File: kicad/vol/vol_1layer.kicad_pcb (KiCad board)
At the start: 2 copper layers, 42 x 26 mm, 6 parts, among them J1 IN L-G-R, J2 OUT L-G-R, J3 LED IN

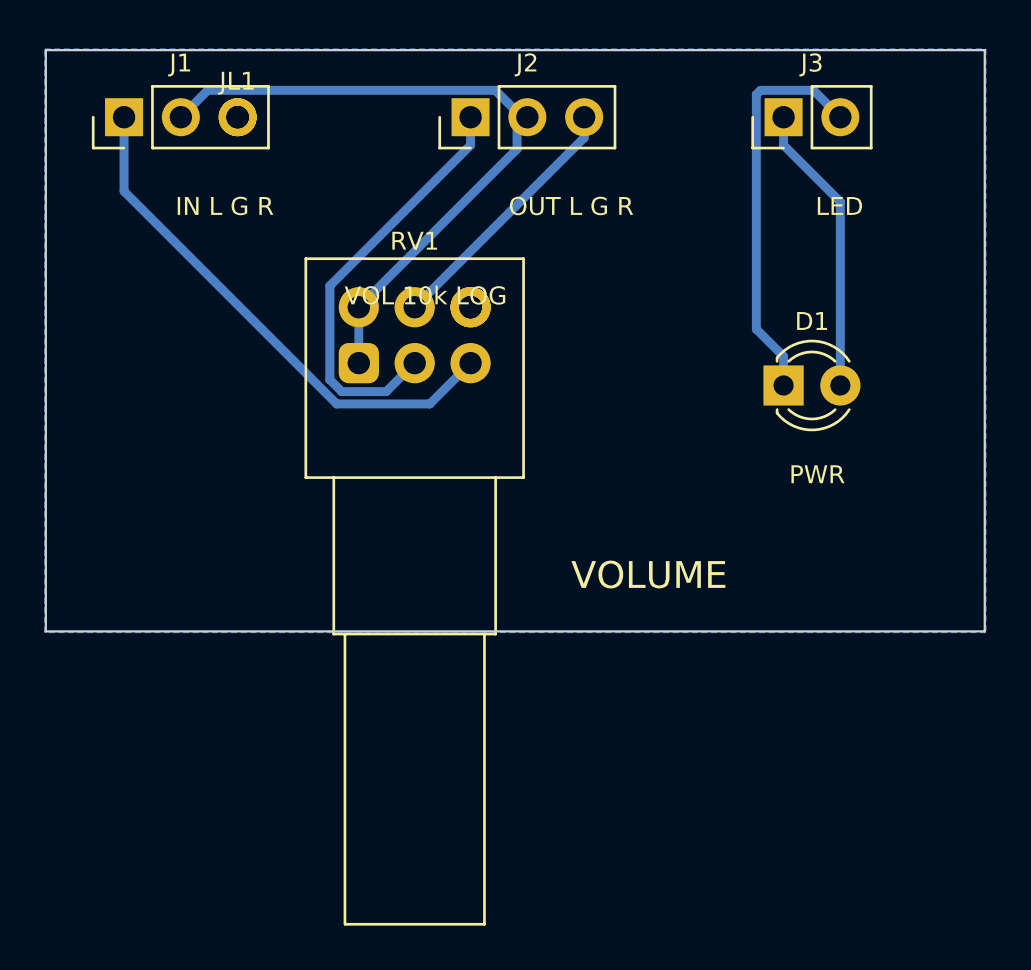
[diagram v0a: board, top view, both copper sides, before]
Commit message: Square 144 x 144 mm panel with rails; amp widened to 134 x 71 mm so PSU plus volume board match its width; readable silkscreen
References sit inside resistor, diode and ceramic outlines along the body axis, larger text; electrolytic,
transistor and test-point labels stay beside the part. Hybrid footprints built from the library parts keep
polarity marks. All 2-layer boards, the panel and the single-sided PSU and volume boards are DRC clean.
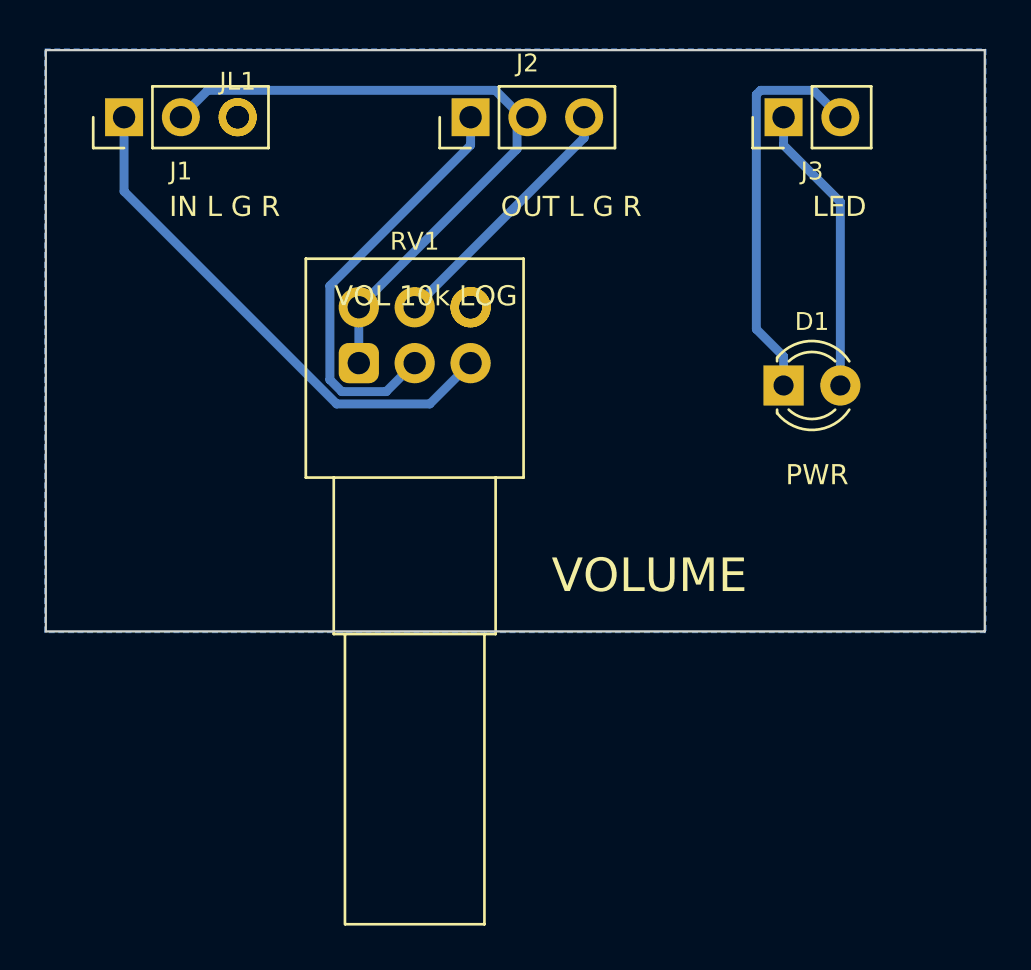
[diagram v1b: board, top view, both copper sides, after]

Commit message: Repository URL and revision on every silkscreen and on the panel rails
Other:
- board text added: "v1.0 2026-10"
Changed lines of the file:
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@@
 		(layer "Edge.Cuts")
+	)
+	(gr_text "v1.0 2026-10"
+		(at 76.95 71.45 0)
+		(layer "F.SilkS")
+		(effects
+			(font
+				(size 0.8 0.8)
+				(thickness 0.12)
+			)
+		)
 	)
 	(gr_text "IN L G R"

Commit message: Release 1.1: square panel, rotated terminals, readable silkscreen, URL and revision stamps
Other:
- board text added: "v1.1 2026-10"
- board text removed: "v1.0 2026-10"
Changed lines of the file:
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@@
 		(layer "Edge.Cuts")
 	)
-	(gr_text "v1.0 2026-10"
+	(gr_text "v1.1 2026-10"
 		(at 76.95 71.45 0)
 		(layer "F.SilkS")

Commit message: Release 1.2: mirror-loaded front end, closed-loop PSU, VU tap, headphone board
- Amp: PNP input pair with NPN current-mirror load, LED-referenced current-source tail,
  NPN VAS with bootstrapped load from +12V, 220p Miller + 47p lead cap (THD 0.004% at 26 mW/8R,
  0.019% at 0.29 W; was 0.03 / 0.2). 1k VU meter tap per channel to header J5.
- PSU: BC547 error amplifier, 5.6 V zener fed from VOUT, 8.2k + 2k trimmer / 10k divider,
  2.2k drive, 47n/100n compensation. 12.0 V set point, 0.14 V dip on a 1 A step.
- New headphone board (DPDT switch, 120R series, DIRECT jumpers, 3.5 mm jack, panel-jack header).
- Boards: amp 134x85 / compact 100x98, PSU 90x58, hp 42x30; panel 155x155 with four boards.
  All 2-layer boards and the panel DRC clean; single-sided amp down to 15 errors.
- Toolchain: STAMP constant, reroute.sh second routing pass, rotated titles, link holes on
  jumper pads, 2 mm routing corridor per channel.
- Docs, BOMs, order guide, changelog, known issues rewritten for release 2.
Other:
- board text added: "v1.2 2026-10"
- board text removed: "v1.1 2026-10"
